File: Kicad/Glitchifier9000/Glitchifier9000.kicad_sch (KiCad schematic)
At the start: 14 parts

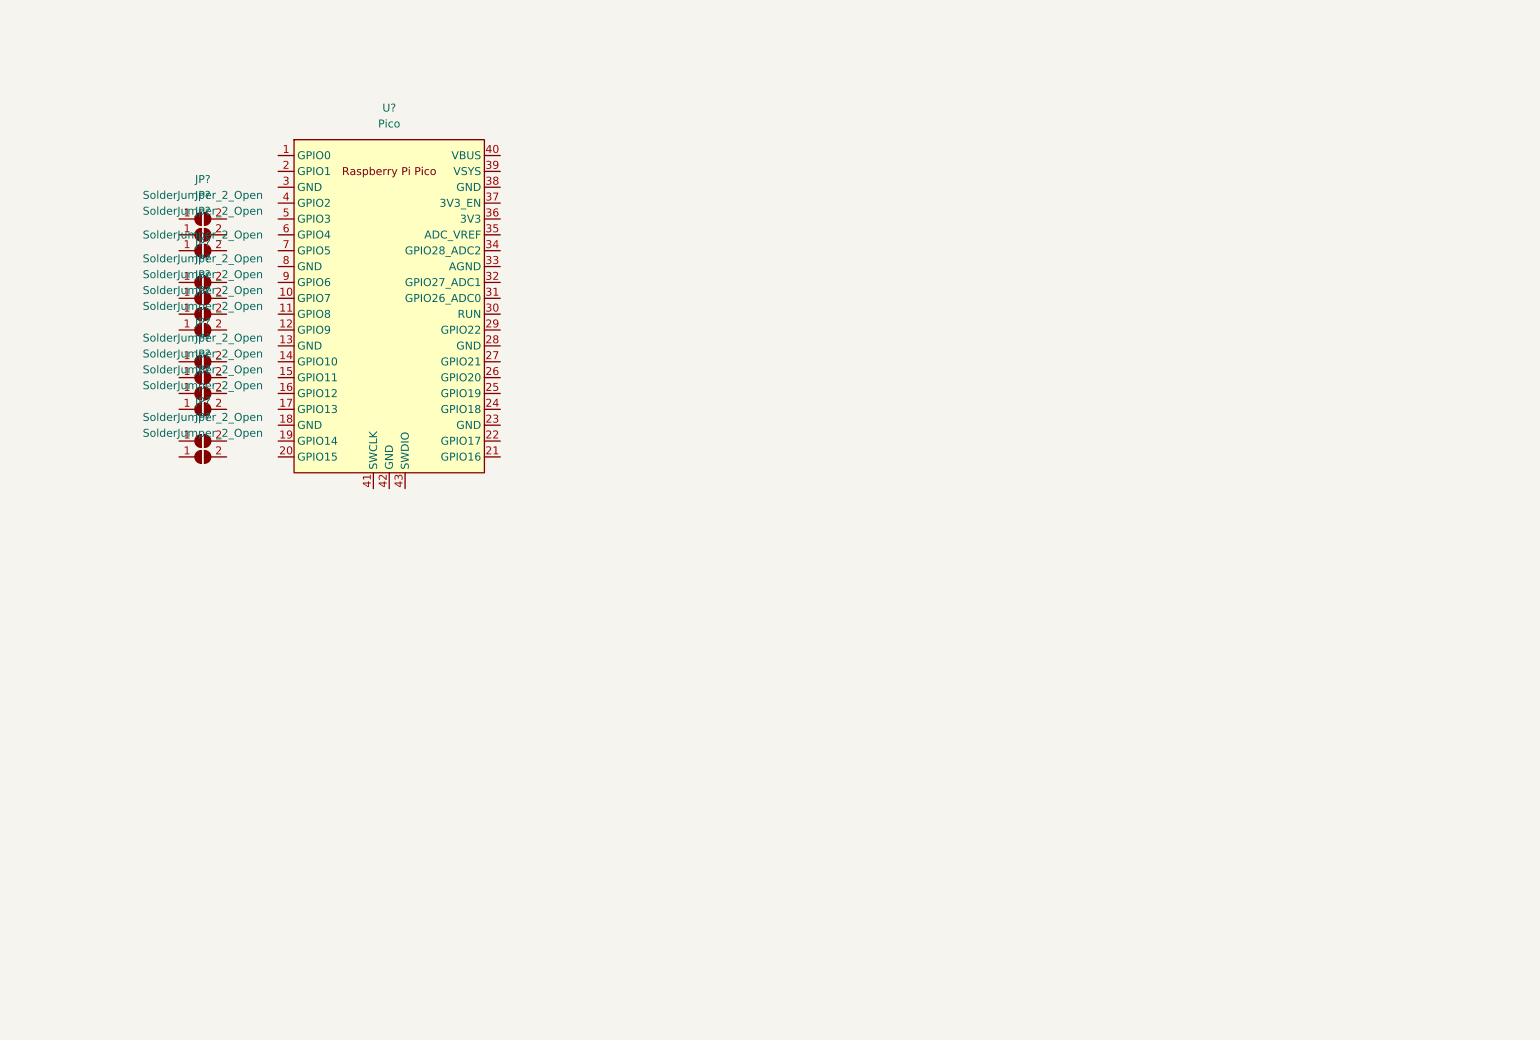
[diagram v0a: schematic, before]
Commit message: Added all basic components to schematic
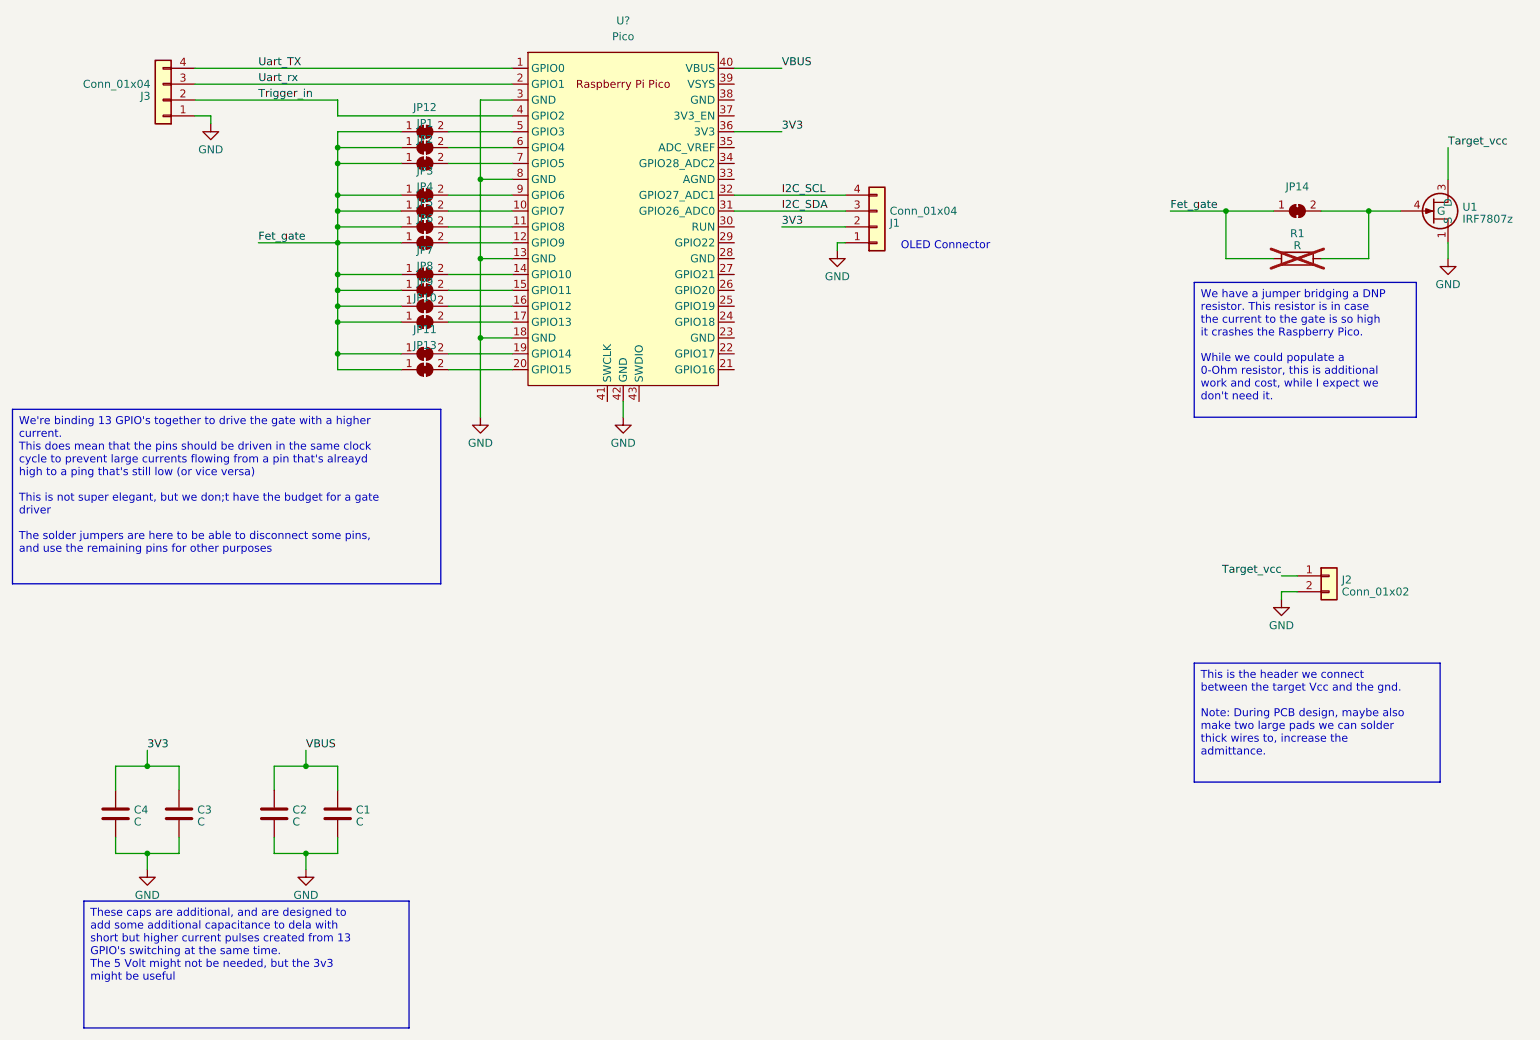
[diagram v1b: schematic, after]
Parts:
- removed JP? (x13): SolderJumper_2_Open, symbol Jumper:SolderJumper_2_Open
- added C1, C2, C3, C4: C, symbol Device:C
- added J1, J3: Conn_01x04, symbol Connector_Generic:Conn_01x04
- added J2: Conn_01x02, symbol Connector_Generic:Conn_01x02
- added JP1, JP10, JP11, JP12, JP13, JP14, JP2, JP3, JP4, JP5, JP6, JP7, JP8, JP9: SolderJumper_2_Bridged, symbol Jumper:SolderJumper_2_Bridged
- added R1: R, symbol Device:R
- added U1: IRF7807z, symbol IRF7807z:IRF7807z
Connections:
- net Uart_TX: now reaches U?.1 (GPIO0)
- net Uart_TX: now also J3.4 (Pin_4)
- net at U?.10 (GPIO7): now also JP4.2 (B)
- net at U?.11 (GPIO8): now also JP5.2 (B)
- net at U?.12 (GPIO9): now also JP6.2 (B)
- net GND: now reaches U?.13 (GND)
- net GND: now also U?.18 (GND), U?.3 (GND), U?.42 (GND), U?.8 (GND), C1.2, C2.2, C3.2, C4.2, J1.1 (Pin_1), J2.2 (Pin_2), J3.1 (Pin_1), U1.1 (S)
- net at U?.14 (GPIO10): now also JP7.2 (B)
- net at U?.15 (GPIO11): now also JP8.2 (B)
- net at U?.16 (GPIO12): now also JP9.2 (B)
- net at U?.17 (GPIO13): now also JP10.2 (B)
- net at U?.19 (GPIO14): now also JP11.2 (B)
- net Uart_rx: now reaches U?.2 (GPIO1)
- net Uart_rx: now also J3.3 (Pin_3)
- net at U?.20 (GPIO15): now also JP13.2 (B)
- net I2C_SDA: now reaches U?.31 (GPIO26_ADC0)
- net I2C_SDA: now also J1.3 (Pin_3)
- net I2C_SCL: now reaches U?.32 (GPIO27_ADC1)
- net I2C_SCL: now also J1.4 (Pin_4)
- net 3V3: now reaches U?.36 (3V3)
- net 3V3: now also C3.1, C4.1, J1.2 (Pin_2)
- net Trigger_in: now reaches U?.4 (GPIO2)
- net Trigger_in: now also J3.2 (Pin_2)
- net VBUS: now reaches U?.40 (VBUS)
- net VBUS: now also C1.1, C2.1
- net at U?.5 (GPIO3): now also JP12.2 (B)
- net at U?.6 (GPIO4): now also JP1.2 (B)
- net at U?.7 (GPIO5): now also JP2.2 (B)
- net at U?.9 (GPIO6): now also JP3.2 (B)
- new net: JP14.2 (B), R1.2, U1.4 (G)
- new net Fet_gate: JP1.1 (A), JP10.1 (A), JP11.1 (A), JP12.1 (A), JP13.1 (A), JP14.1 (A), JP2.1 (A), JP3.1 (A), JP4.1 (A), JP5.1 (A), JP6.1 (A), JP7.1 (A), JP8.1 (A), JP9.1 (A), R1.1
- new net Target_vcc: J2.1 (Pin_1), U1.3 (D)
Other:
- note added: "OLED Connector"
- moved on the sheet: U?
